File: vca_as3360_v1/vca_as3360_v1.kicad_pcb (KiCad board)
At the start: 2 copper layers, 30 x 100 mm, 71 parts, among them J1 Conn_02x05_Odd_Even, J2 OUT_1, J3 OUT_2, J4 CV1, J5 CV2, J6 IN1, J7 IN2, Q1 BC547, Q2 BC547, U1 AS3360, U2 TL072, U3 TL072, U4 TL072

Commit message: Layout and routing first pass done
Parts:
- removed C8, C9: 10nF, Capacitor_SMD:C_1206_3216Metric_Pad1.33x1.80mm_HandSolder
- added R31: 10k, Resistor_SMD:R_1206_3216Metric_Pad1.30x1.75mm_HandSolder, B.Cu at (162.9, 79.8)
- added R32: 100k, Resistor_SMD:R_1206_3216Metric_Pad1.30x1.75mm_HandSolder, B.Cu at (166.8, 81.3)
- C4, C5: moved to F.Cu
- D4, D6, Q2, R1, R10, R12, R13, R14, R15, R17, R18, R19, R2, R21, R22, R23, R24, R26, R27, R28, R29, R3, R30, R4, R5, R6, R7, R8, R9: moved to B.Cu
- R11, R20: value R -> 1k; moved to B.Cu
- R16: value 90k -> 100k; moved to B.Cu
- R25: value 90k -> 10k; moved to B.Cu
- U3: value TL072 -> LM358
- moved C6 121.6 mm to (149.5, 96.4)
- moved R22 120.0 mm to (152.1, 144.1), turned to -90 degrees
- moved C7 117.8 mm to (149.5, 98.8)
- moved C3 111.4 mm to (161.5, 96.5), turned to 180 degrees
- moved R21 109.8 mm to (156.4, 137.4), turned to 180 degrees
- moved D6 105.6 mm to (152.0, 137.3), turned to -90 degrees
- moved R23 101.2 mm to (151.9, 133.4), turned to -90 degrees
- moved R2 98.2 mm to (173.3, 119.2), turned to 180 degrees
- moved R4 95.5 mm to (168.2, 116.7), turned to 180 degrees
- moved U1 94.9 mm to (163.0, 101.4), turned to 90 degrees
- moved R7 94.1 mm to (173.7, 103.1), turned to 180 degrees
- moved R14 92.8 mm to (158.9, 118.3), turned to 180 degrees
- moved R10 90.0 mm to (170.6, 100.4), turned to 180 degrees
- moved C10 89.9 mm to (173.7, 108.9)
- moved R5 89.9 mm to (173.3, 116.7), turned to 180 degrees
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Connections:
- R25 pad 1: -12V -> Net-(R16-Pad2)
- R25 pad 2: Net-(R25-Pad2) -> Net-(RV1-Pad1)
- RV1 pad 1: Net-(R16-Pad2) -> Net-(RV1-Pad1)
- RV2 pad 1: Net-(R25-Pad2) -> Net-(RV2-Pad1)
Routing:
- net +12V: track 0.00 -> 171.7 mm, vias 0 -> 3
- net -12V: track 0.00 -> 130.0 mm, vias 0 -> 1
- net Net-(J4-PadT): track 0.00 -> 88.2 mm, vias 0 -> 1
- net Net-(RV2-Pad2): track 0.00 -> 80.0 mm, vias 0 -> 1
- net Net-(J7-PadT): track 0.00 -> 68.2 mm
- net Net-(J6-PadT): track 0.00 -> 43.8 mm
- net Net-(J3-PadT): track 0.00 -> 38.6 mm
- net /intput_block/Signal_2: track 0.00 -> 29.7 mm
- net /intput_block/Linear CV 2: track 0.00 -> 23.3 mm
- net Net-(R23-Pad1): track 0.00 -> 21.4 mm
- net /output_block/OUT_A_BUF: track 0.00 -> 19.5 mm
- net Net-(R14-Pad1): track 0.00 -> 16.5 mm
- net /intput_block/Signal_1: track 0.00 -> 16.3 mm
- net /intput_block/Linear CV 1: track 0.00 -> 12.0 mm
- net Net-(R10-Pad2): track 0.00 -> 11.8 mm
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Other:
- board size 30 x 100 mm -> 38 x 100 mm
- board text added: "Could put connector here to pass power to another board making 4 x VCA"
- board text added: "HP Inch mm 1 0.2 5.08 2 0.4 10.16 3 0.6 15.24 4 0.8 20.32 5 1 25.4 6 1.2 30.48 7 1.4 35.56 8 1.6 40.64 9 1.8 45.72 10 2 50.8 11 2.2 55.88 12 2.4 60.96 13 2.6 66.04 14 2.8 71.12 15 3 76.2 16 3.2 81.28 17 3.4 86.36 18 3.6 91.44 19 3.8 96.52 20 4 101.6 21 4.2 106.68 22 4.4 111.76 23 4.6 116.84 24 4.8 121.92 25 5 127 26 5.2 132.08 27 5.4 137.16 28 5.6 142.24 29 5.8 147.32 30 6 152.4"

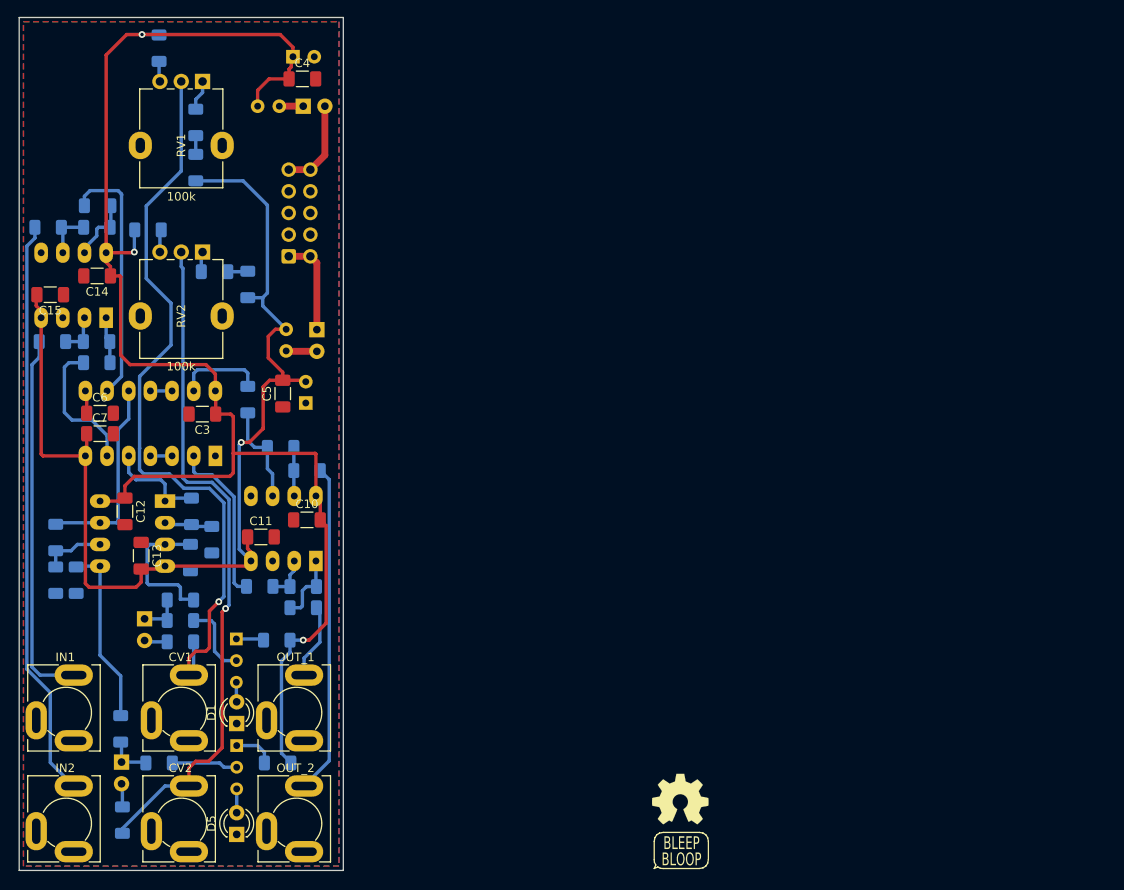
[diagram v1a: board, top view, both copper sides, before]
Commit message: Geographic rename and silkscreen cleanup
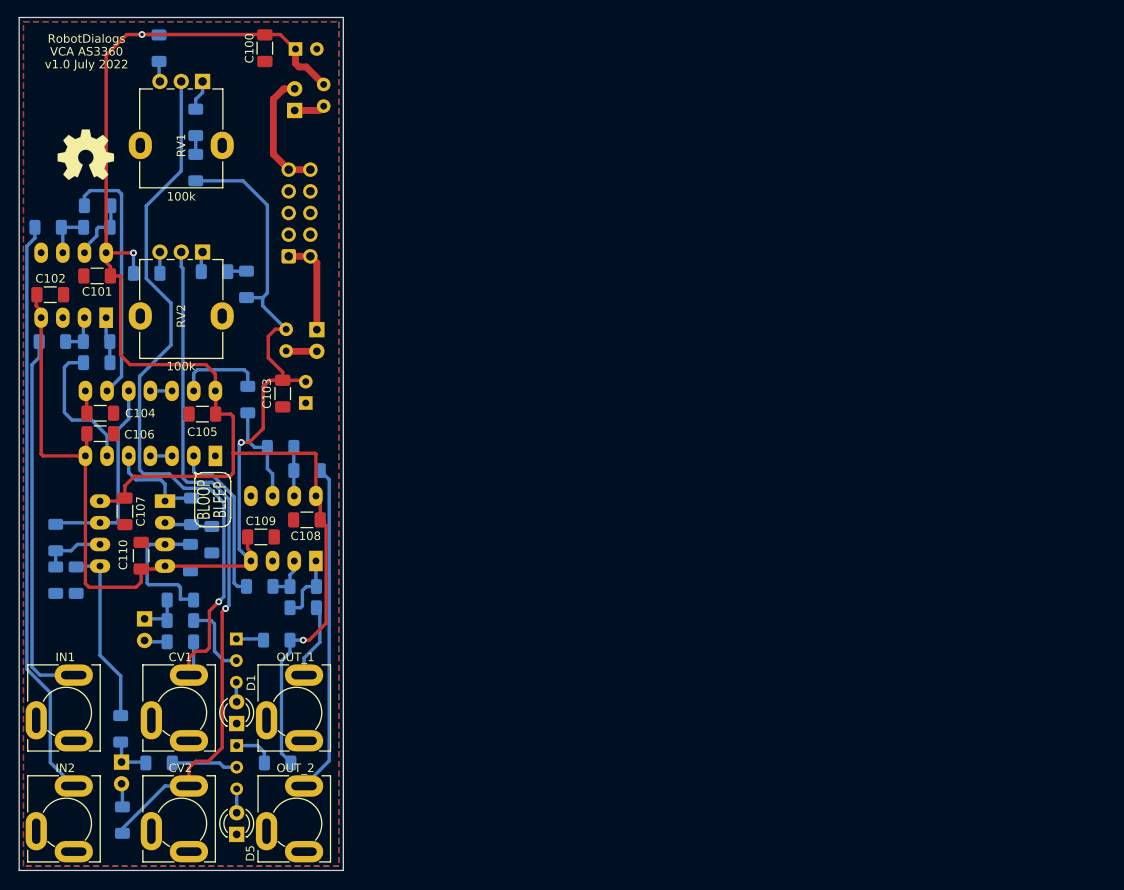
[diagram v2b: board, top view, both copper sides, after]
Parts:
- moved LOGO100 102.8 mm to (147.8, 66.1)
- moved LOGO102 83.1 mm to (159.8, 88.0), turned to -45 degrees
- moved LOGO101 68.6 mm to (162.7, 106.5), turned to -90 degrees
- moved C100 5.69 mm to (168.8, 53.6), turned to -90 degrees
- moved FB1 5.21 mm to (175.7, 60.4), turned to 90 degrees
- moved R8 5.10 mm to (154.9, 80.0)
- moved D2 1.12 mm to (172.3, 60.9), turned to 90 degrees
- moved C2 0.95 mm to (172.4, 53.7)
- moved R9 0.15 mm to (166.7, 81.3)
- renumbered C4 to C100, C14 to C101, C15 to C102, C5 to C103, C6 to C104, C3 to C105, C7 to C106, C12 to C107, C10 to C108, C11 to C109, C13 to C110, C1 to C2, C2 to C3, D3 to D2, D2 to D3, FB2 to FB1, FB1 to FB2, J1 to J8, LOGO3 to LOGO100, LOGO1 to LOGO101, LOGO2 to LOGO102, R15 to R1, R6 to R10, R3 to R11, R1 to R12, R9 to R13, R10 to R14, R7 to R15, R19 to R16, R18 to R17, R28 to R18, R17 to R19, R25 to R2, R26 to R20, R27 to R21, R5 to R22, R4 to R23, R14 to R24, R2 to R25, R12 to R26, R11 to R27, R13 to R28, R23 to R29, R16 to R3, R20 to R30, R21 to R31, R22 to R32, R30 to R4, R29 to R5, R8 to R6, R31 to R7, R24 to R8, R32 to R9, U4 to U1, U1 to U2, U2 to U4
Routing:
- net +12V: track 171.7 -> 167.4 mm
- net +12VA: track 10.7 -> 14.5 mm
- net Net-(D2-Pad1): track 2.81 -> 3.61 mm
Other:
- board text added: "AS3360"
- board text added: "CV1"
- board text added: "CV2"
- board text added: "IN1"
- board text added: "IN2"
- board text added: "LM358"
- board text added: "OUT1"
- board text added: "OUT2"
- board text added: "TL072"
- board text added: "VCA AS3360"
- board text added: "v1.0 July 2022"
- board text removed: "Eurorack Template"
- board text removed: "v1.1 July 2022"

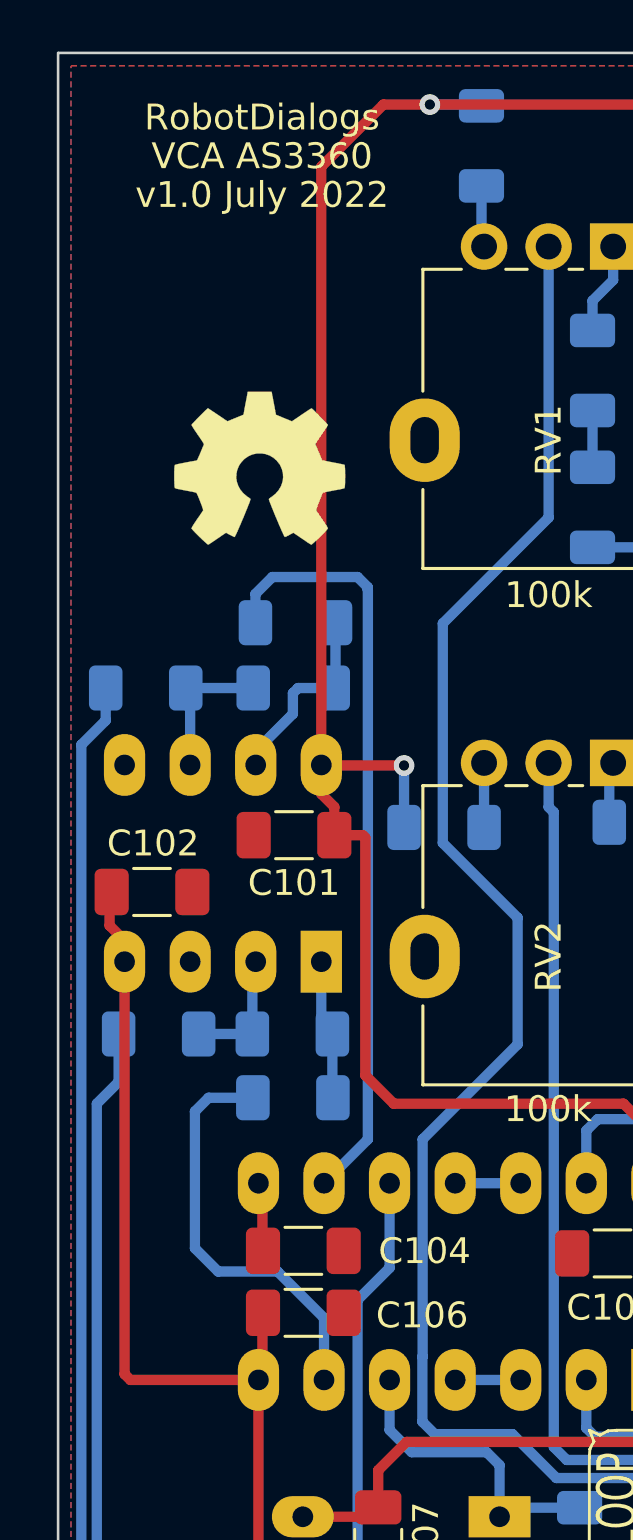
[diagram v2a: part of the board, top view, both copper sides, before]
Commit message: Add jumper points for passing power to another pcb
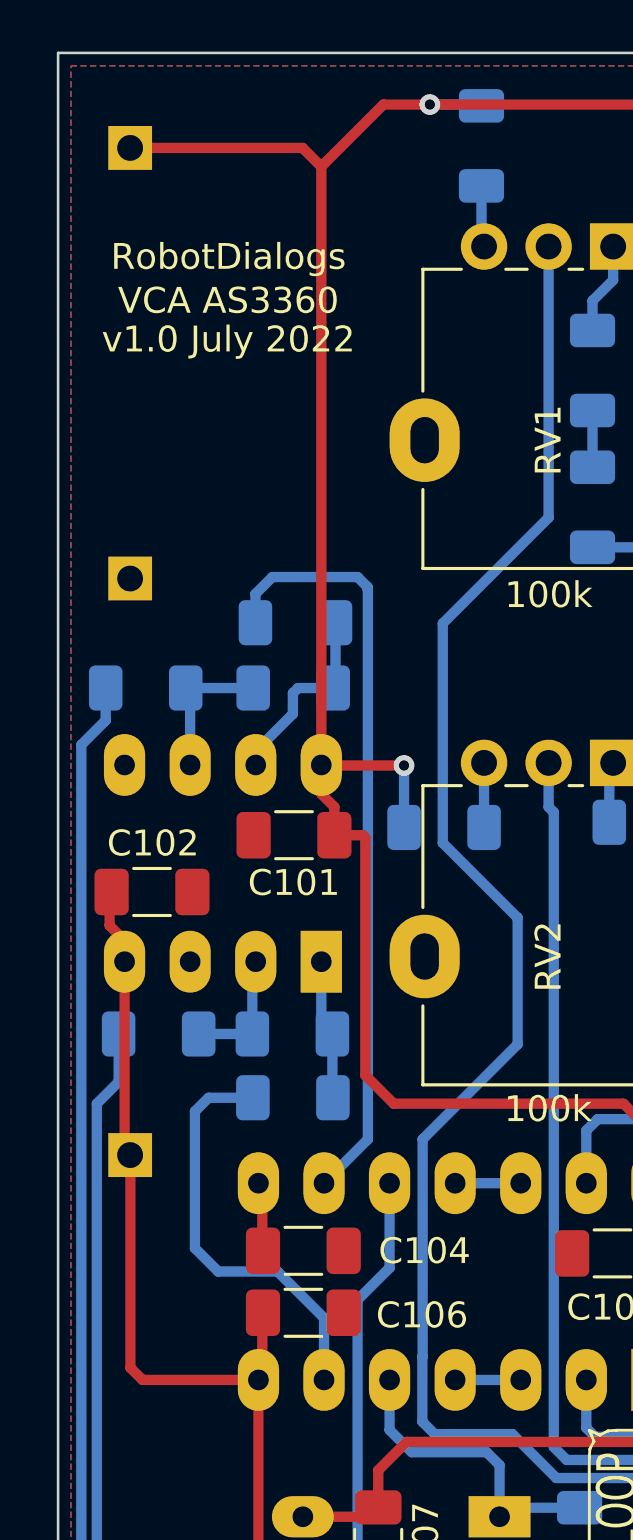
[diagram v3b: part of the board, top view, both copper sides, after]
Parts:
- added J1: +12V, Connector_PinHeader_2.54mm:PinHeader_1x01_P2.54mm_Vertical, B.Cu at (142.8, 53.7)
- added J10: GND, Connector_PinHeader_2.54mm:PinHeader_1x01_P2.54mm_Vertical, B.Cu at (142.8, 70.4)
- added J9: -12V, Connector_PinHeader_2.54mm:PinHeader_1x01_P2.54mm_Vertical, B.Cu at (142.8, 92.7)
- LOGO100: moved to B.Cu
- moved LOGO100 0.71 mm to (148.5, 66.0), turned to 180 degrees
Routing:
- net +12V: track 167.4 -> 175.1 mm
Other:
- board text added: "40.64 = 8HP"
- board text added: "Power connectors this side to pass power to another board making 4 x VCA"
- board text removed: "15.24 = 3HP"
- board text removed: "Could put connector here to pass power to another board making 4 x VCA"
